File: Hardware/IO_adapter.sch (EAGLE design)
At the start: 56 parts, among them Y1 32Khz

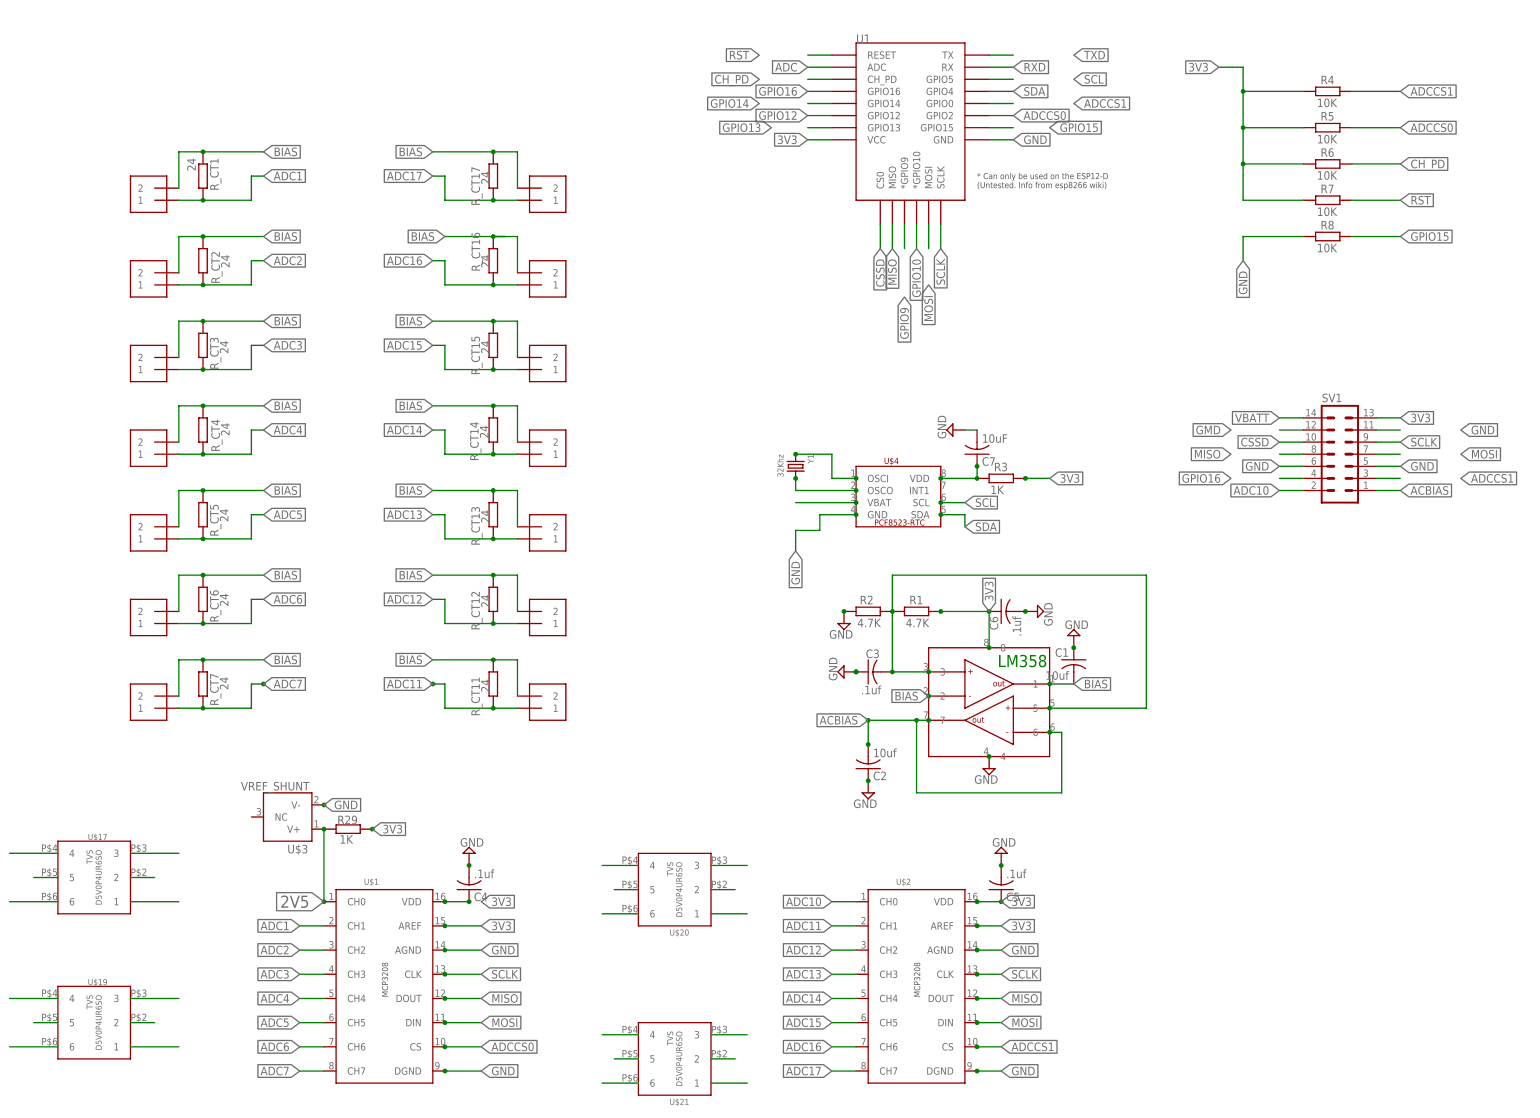
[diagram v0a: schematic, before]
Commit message: initial redesign
design for the Italtronic 3M modular case series
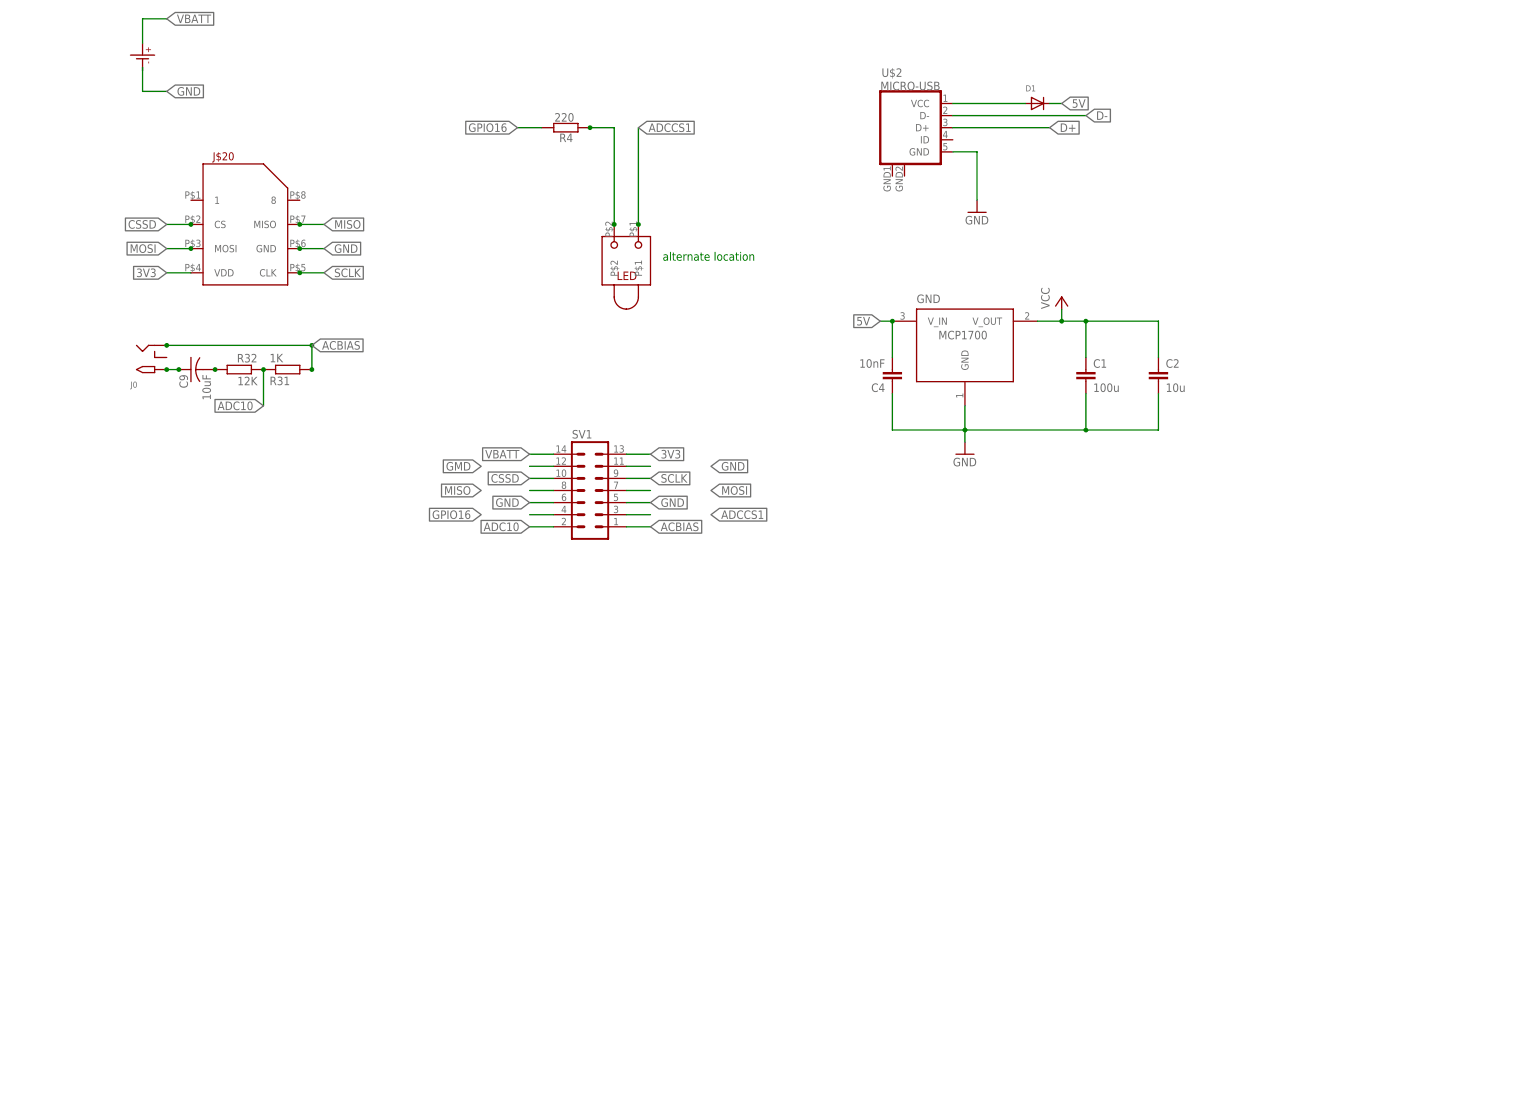
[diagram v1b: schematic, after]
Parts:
- removed C3, C5, C6: .1uf, adafruit:C-USC0805
- removed C7: 10uF, adafruit:C-USC0805
- removed CT1, CT11, CT12, CT13, CT14, CT15, CT16, CT17, CT2, CT3, CT4, CT5, CT6, CT7: 1X2-3.5MM, adafruit:1X2-3.5MM
- removed R1, R2: 4.7K, resistor:R-EU_R0805
- removed R29, R3: 1K, resistor:R-EU_R0805
- removed R5, R6, R7, R8: 10K, resistor:R-EU_R0805
- removed R_CT1, R_CT11, R_CT12, R_CT13, R_CT14, R_CT15, R_CT16, R_CT17, R_CT2, R_CT3, R_CT4, R_CT5, R_CT6, R_CT7: 24, resistor:R-EU_R0805
- removed U$17, U$19, U$20, U$21: TVS_4CHAN_ARRAYSC-74, IotaWatt_parts:TVS_4CHAN_ARRAYSC-74
- removed U$22: LM358_DUAL_OP-AMP, IotaWatt_parts:LM358_DUAL_OP-AMP
- removed U$3: VREF_SHUNT, IotaWatt_parts:VREF_SHUNT
- removed U$4: PCF8523_RTC, IotaWatt_parts:PCF8523_RTC
- removed U1: (no value), esp8266modules:ESP12ESMD
- removed Y1: 32Khz, microbuilder:CRYSTAL8X3.8SMT
- added C9: 10uF, adafruit:C-USC0805
- added D1: (no value), adafruit:DIODESOD-323F
- added GND: MCP1700SOT23, MCP1700:MCP1700SOT23
- added J$20: MICROSD_PUSH/PULL, IotaWatt_parts:MICROSD_PUSH/PULL
- added J0: 2.1MMJACKSMT, IotaWatt_parts:2.1MMJACKSMT
- added R31: 1K, resistor:R-EU_R0805
- added R32: 12K, resistor:R-EU_R0805
- added U$23: LED_RT_TRH, IotaWatt_parts:LED_RT_TRH
- C1: value 10uf -> 100u; device adafruit:C-USC0805 -> eagle-ltspice:C
- C2: value 10uf -> 10u; device adafruit:C-USC0805 -> eagle-ltspice:C
- C4: value .1uf -> 10nF; device adafruit:C-USC0805 -> eagle-ltspice:C
- R4: value 10K -> 220
- U$1: value MCP3208 -> CR1220SMD; device IotaWatt_parts:MCP3208 -> IotaWatt4.8:CR1220SMD
- U$2: value MCP3208 -> MICRO-USB; device IotaWatt_parts:MCP3208 -> microusb (1):MICRO-USB
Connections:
- removed net 2V5: R29.2, U$1.CH0, U$3.V+
- removed net ADC: U1.ADC
- removed net ADC1: CT1.1, R_CT1.2, U$1.CH1, U$17.3
- removed net ADC11: CT11.1, R_CT11.2, U$2.CH1, U$20.4
- removed net ADC12: CT12.1, R_CT12.2, U$2.CH2, U$20.3
- removed net ADC13: CT13.1, R_CT13.2, U$2.CH3, U$20.1
- removed net ADC14: CT14.1, R_CT14.2, U$2.CH4, U$21.3
- removed net ADC15: CT15.1, R_CT15.2, U$2.CH5, U$21.1
- removed net ADC16: CT16.1, R_CT16.2, U$2.CH6, U$21.6
- removed net ADC17: CT17.1, R_CT17.2, U$2.CH7, U$21.4
- removed net ADC2: CT2.1, R_CT2.2, U$1.CH2, U$17.1
- removed net ADC3: CT3.1, R_CT3.2, U$1.CH3, U$17.6
- removed net ADC4: CT4.1, R_CT4.2, U$1.CH4, U$17.4
- removed net ADC5: CT5.1, R_CT5.2, U$1.CH5, U$19.4
- removed net ADC6: CT6.1, R_CT6.2, U$1.CH6, U$19.3
- removed net ADC7: CT7.1, R_CT7.2, U$1.CH7, U$19.1
- removed net ADCCS0: R5.2, U$1.CS, U1.GPIO2
- removed net BIAS: C1.2, CT1.2, CT11.2, CT12.2, CT13.2, CT14.2, CT15.2, CT16.2, CT17.2, CT2.2, CT3.2, CT4.2, CT5.2, CT6.2, CT7.2, R_CT1.1, R_CT11.1, R_CT12.1, R_CT13.1, R_CT14.1, R_CT15.1, R_CT16.1, R_CT17.1, R_CT2.1, R_CT3.1, R_CT4.1, R_CT5.1, R_CT6.1, R_CT7.1, U$22.1, U$22.2
- removed net CH_PD: R6.2, U1.CH_PD
- removed net GPIO10: U1.*GPIO10
- removed net GPIO12: U1.GPIO12
- removed net GPIO13: U1.GPIO13
- removed net GPIO14: U1.GPIO14
- removed net GPIO15: R8.2, U1.GPIO15
- removed net GPIO9: U1.*GPIO9
- removed net N$1: C7.1, R3.1, U$4.VDD
- removed net N$44: U$4.OSCO, Y1.2
- removed net N$45: U$4.OSCI, Y1.1
- removed net N$7: U$19.6
- removed net RST: R7.2, U1.RESET
- removed net RXD: U1.RX
- removed net SCL: U$4.SCL, U1.GPIO5
- removed net SDA: U$4.SDA, U1.GPIO4
- removed net TXD: U1.TX
- removed net VREF: C3.2, R1.1, R2.2, U$22.3, U$22.5
- new net 5V: C4.2, D1.C, GND.V_IN
- new net 5VUSB: D1.A, U$2.VCC
- new net D+: U$2.D+
- new net D-: U$2.D-
- new net N$17: C9.2, R32.2
- new net N$27: C9.1, J0.TIP
- new net N$8: R4.1, U$23.P$2
- net 3V3: now also C1.1, C2.1, GND.V_OUT, J$20.VDD; no longer C4.1, C5.1, C6.1, R1.2, R29.1, R3.2, R4.1, R5.1, R6.1, R7.1, U$1.AREF, U$1.VDD, U$17.5, U$19.5, U$2.AREF, U$2.VDD, U$20.5, U$21.5, U$22.8, U1.VCC
- net ACBIAS: now also J0.RING, R31.2; no longer C2.2, U$22.6, U$22.7
- net ADC10: now also R31.1, R32.1; no longer U$2.CH0, U$20.6
- net ADCCS1: now also U$23.P$1; no longer R4.2, U$2.CS, U1.GPIO0
- net CSSD: now also J$20.CS; no longer U1.CS0
- net GND: now also C1.2, C2.2, C4.1, GND.GND, J$20.GND, U$2.GND; no longer C1.1, C2.1, C3.1, C4.2, C5.2, C6.2, C7.2, R2.1, R8.1, U$1.AGND, U$1.DGND, U$17.2, U$19.2, U$2.AGND, U$2.DGND, U$20.2, U$21.2, U$22.4, U$3.V-, U$4.GND, U1.GND
- net GPIO16: now also R4.2; no longer U1.GPIO16
- net MISO: now also J$20.MISO; no longer U$1.DOUT, U$2.DOUT, U1.MISO
- net MOSI: now also J$20.MOSI; no longer U$1.DIN, U$2.DIN, U1.MOSI
- net SCLK: now also J$20.CLK; no longer U$1.CLK, U$2.CLK, U1.SCLK
- net VBATT: now also U$1.P$+; no longer U$4.VBAT
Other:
- note added: "alternate location"
- note removed: "LM358"
- moved on the sheet: C1, C2, C4, R4, SV1
